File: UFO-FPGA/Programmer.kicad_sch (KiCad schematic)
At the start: 41 parts, among them U2 FT2232HL, U3 ASDMB-12MHz

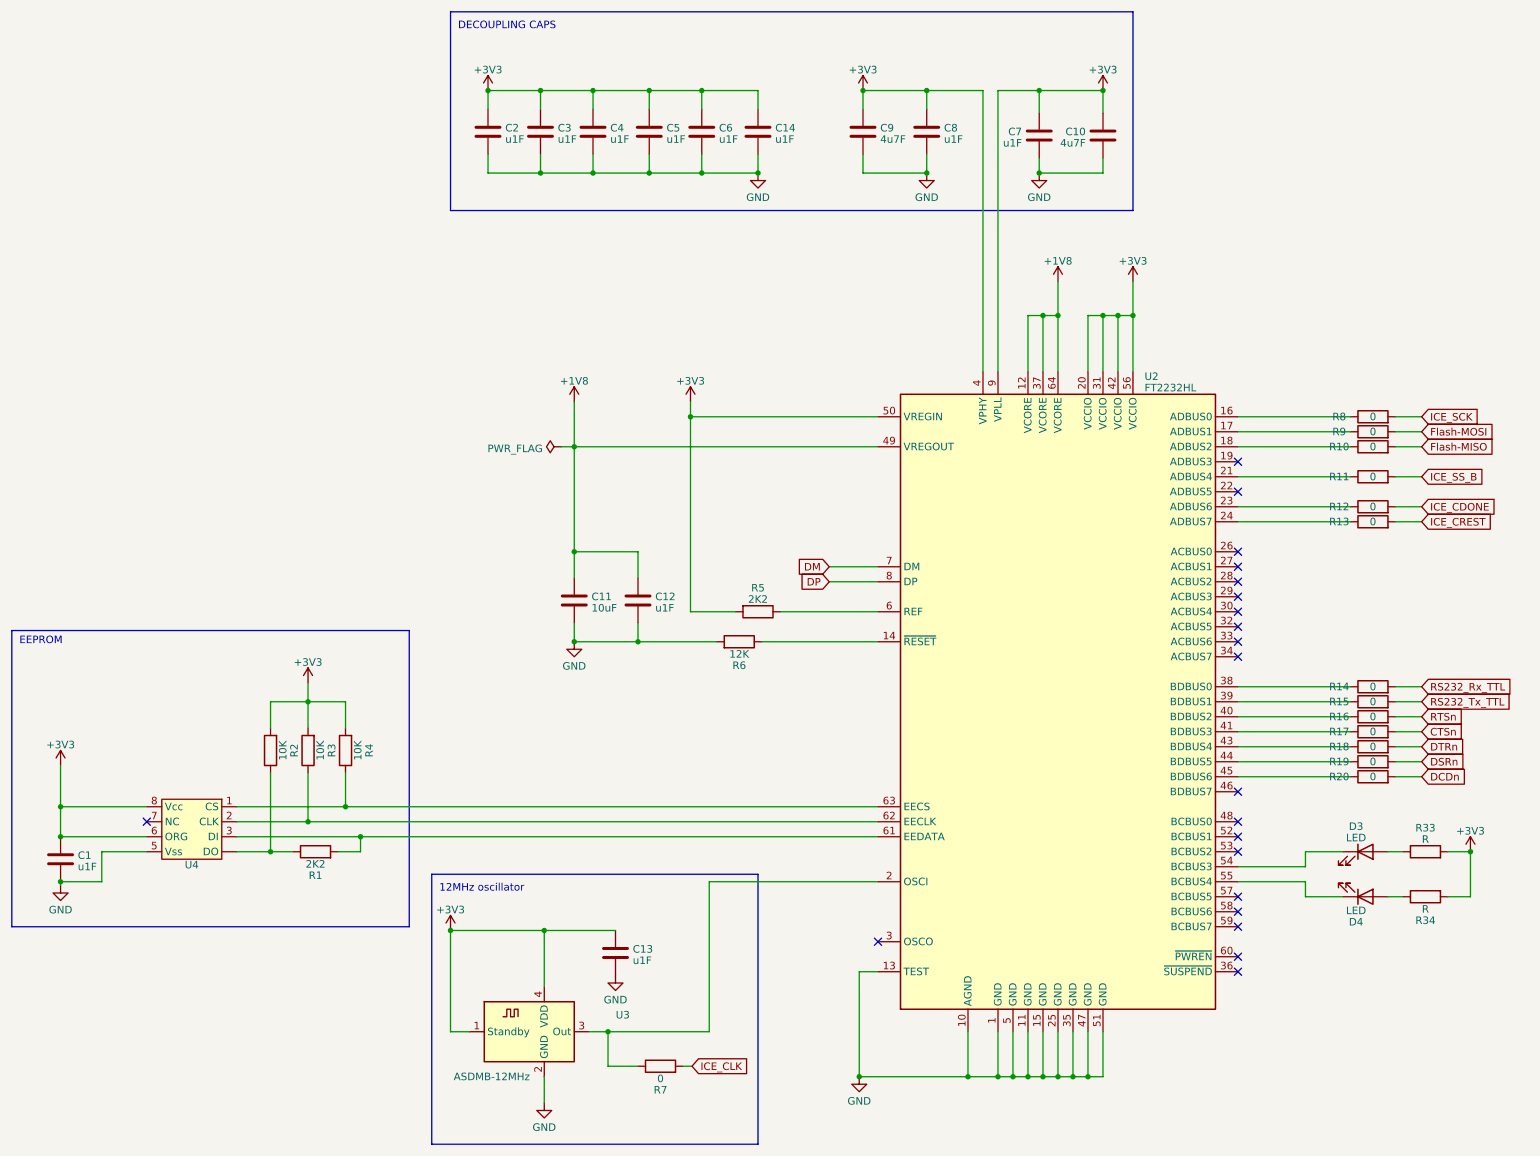
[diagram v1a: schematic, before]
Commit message: Labels and schametic changes
Updated Power schematic
Added labes for the different nets
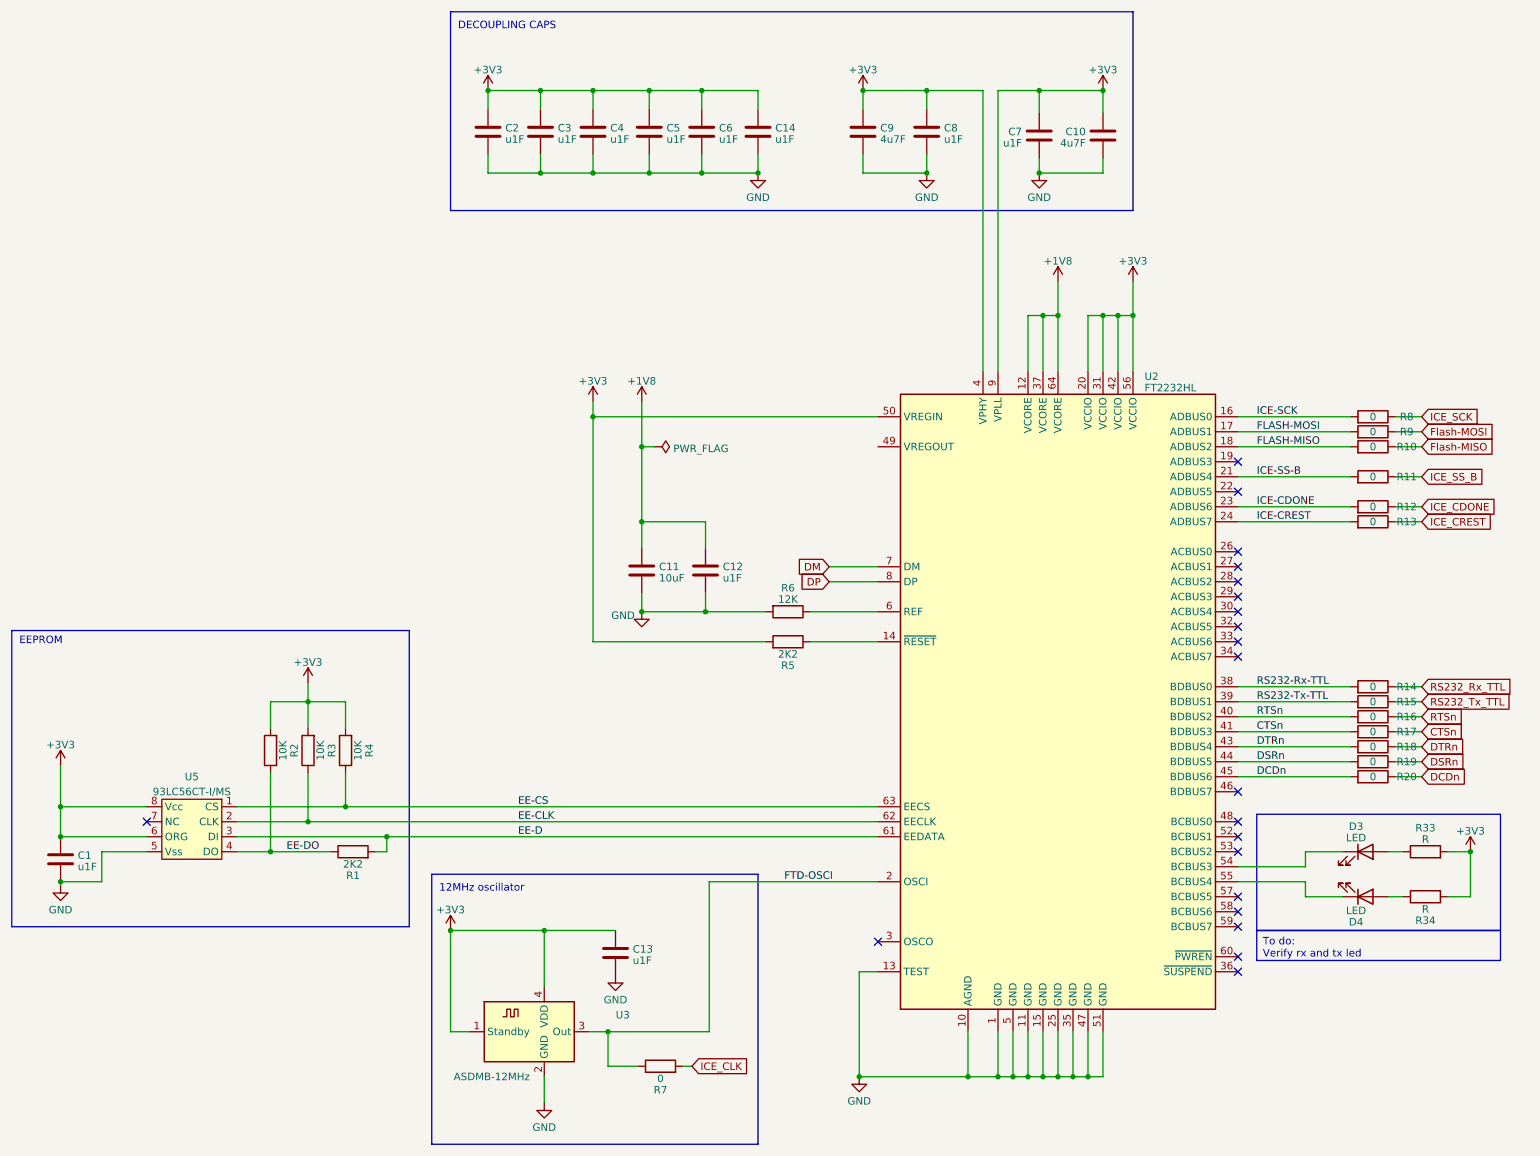
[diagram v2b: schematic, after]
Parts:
- removed U4: ~, Package_SO:MSOP-8-1EP_3x3mm_P0.65mm_EP1.68x1.88mm, symbol EXTRA-PARTS:93LC56CT-I/MS
- added U5: 93LC56CT-I/MS, symbol UFO_PARTS:93LC56CT-I/MS
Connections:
- net +1V8: no longer U2.49 (VREGOUT)
- net +3V3: now also U5.6 (ORG), U5.8 (Vcc)
- net CTSn: now also R17.1, U2.41 (BDBUS3)
- net DCDn: now also R20.1, U2.45 (BDBUS6)
- net DSRn: now also R19.1, U2.44 (BDBUS5)
- net DTRn: now also R18.1, U2.43 (BDBUS4)
- net Flash-MISO: now also R10.1; no longer R10.2
- net Flash-MOSI: now also R9.1; no longer R9.2
- net GND: now also U5.5 (Vss)
- net ICE_CDONE: now also R12.1; no longer R12.2
- net ICE_CREST: now also R13.1; no longer R13.2
- net ICE_SCK: now also R8.1; no longer R8.2
- net ICE_SS_B: now also R11.1; no longer R11.2
- net RS232_Rx_TTL: now also R14.1; no longer R14.2
- net RS232_Tx_TTL: now also R15.1; no longer R15.2
- net RTSn: now also R16.1, U2.40 (BDBUS2)
- net ICE-CREST: now reaches U2.24 (ADBUS7)
- net ICE-CREST: now also R13.2; no longer R13.1
- net RS232-Tx-TTL: now reaches U2.39 (BDBUS1)
- net RS232-Tx-TTL: now also R15.2; no longer R15.1
- net ICE-SS-B: now reaches U2.21 (ADBUS4)
- net ICE-SS-B: now also R11.2; no longer R11.1
- net RS232-Rx-TTL: now reaches U2.38 (BDBUS0)
- net RS232-Rx-TTL: now also R14.2; no longer R14.1
- net EE-DO: now reaches R1.1, R2.1
- net EE-DO: now also U5.4 (DO)
- net EE-D: now reaches R1.2, U2.61 (EEDATA)
- net EE-D: now also U5.3 (DI)
- net FLASH-MOSI: now reaches U2.17 (ADBUS1)
- net FLASH-MOSI: now also R9.2; no longer R9.1
- net FLASH-MISO: now reaches U2.18 (ADBUS2)
- net FLASH-MISO: now also R10.2; no longer R10.1
- net ICE-SCK: now reaches U2.16 (ADBUS0)
- net ICE-SCK: now also R8.2; no longer R8.1
- net at R6.1: now also U2.6 (REF); no longer U2.14 (~{RESET})
- net FTD-OSCI: now reaches R7.1, U2.2 (OSCI), U3.3 (Out)
- net ICE-CDONE: now reaches U2.23 (ADBUS6)
- net ICE-CDONE: now also R12.2; no longer R12.1
- net at R5.1: now also U2.14 (~{RESET}); no longer U2.6 (REF)
- net EE-CS: now reaches R4.1, U2.63 (EECS)
- net EE-CS: now also U5.1 (CS)
- net EE-CLK: now reaches R3.1, U2.62 (EECLK)
- net EE-CLK: now also U5.2 (CLK)
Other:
- moved on the sheet: C11, C12, R1, R10, R11, R12, R13, R14, R15, R16, R17, R18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

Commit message: Revision
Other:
- company: (none) -> Universal-Field-Objects
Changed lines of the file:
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@@
   (paper "A3")
   (title_block
-    (date "2023-04-22")
-    (rev "V0.1")
+    (date "2023-04-25")
+    (rev "V0.5")
+    (company "Universal-Field-Objects")
   )
   (junction (at 264.16 64.135) (diameter 0) (color 0 0 0 0)

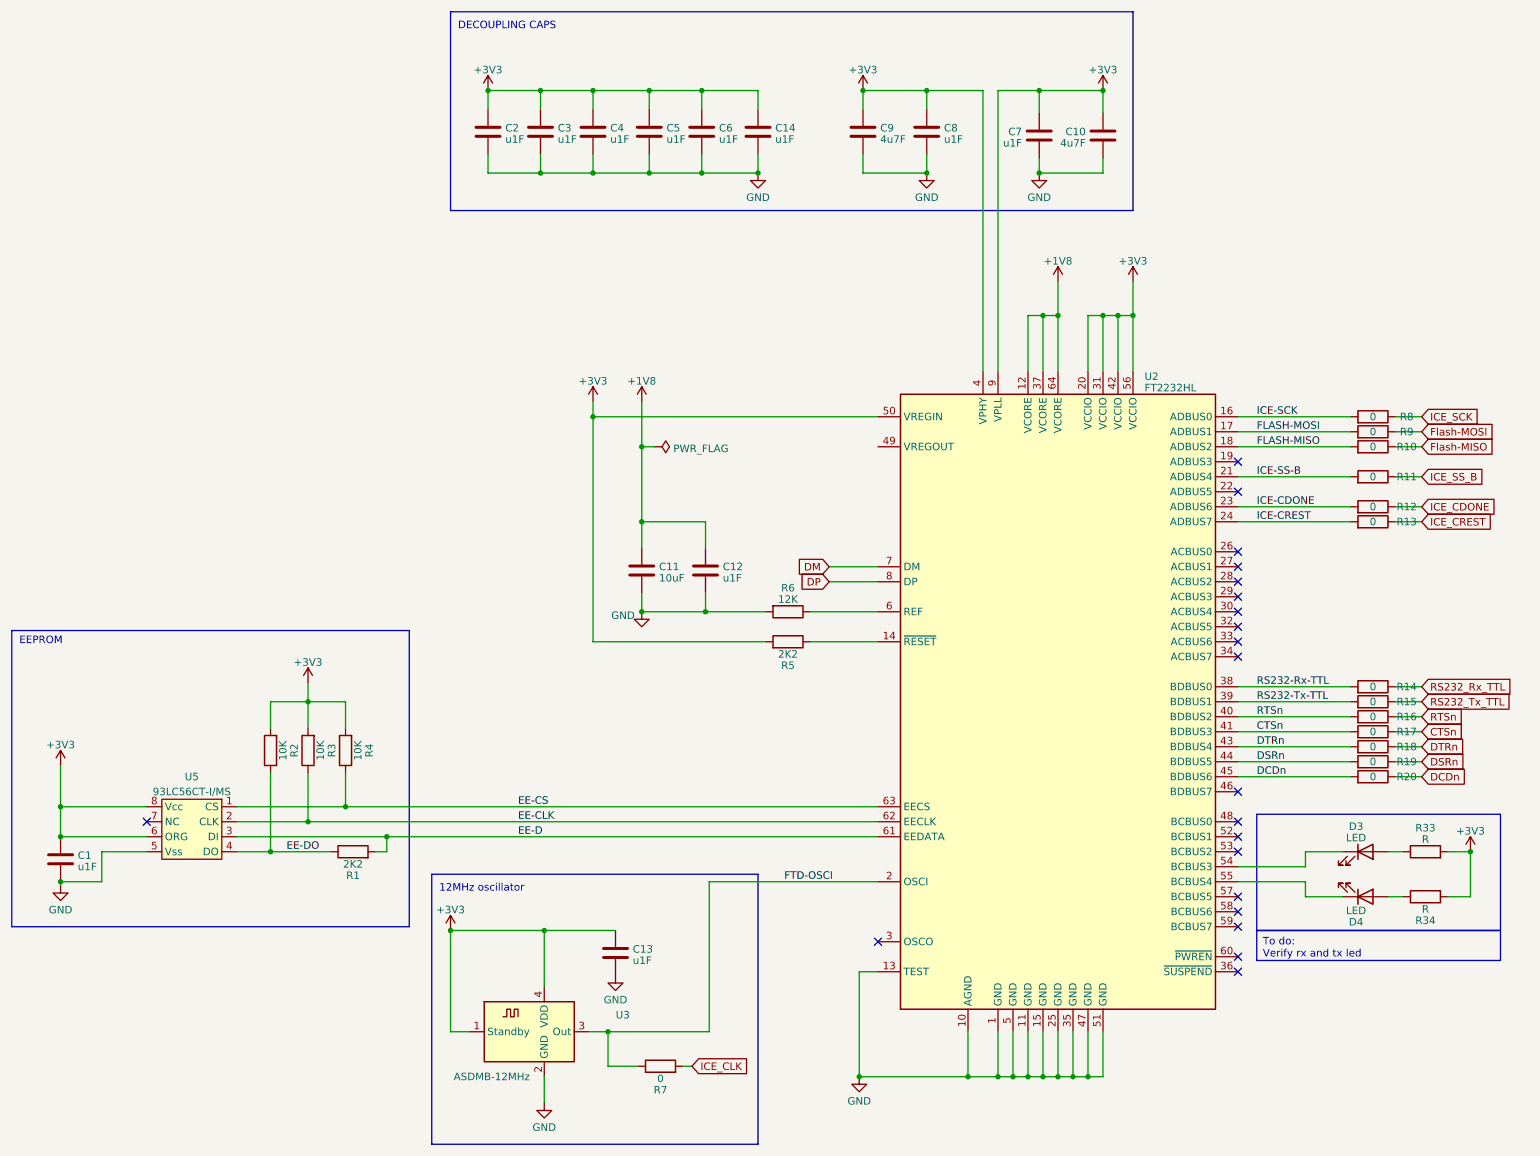
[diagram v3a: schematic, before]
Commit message: PCB and footprint
Added foorprints and moved on pcb layout
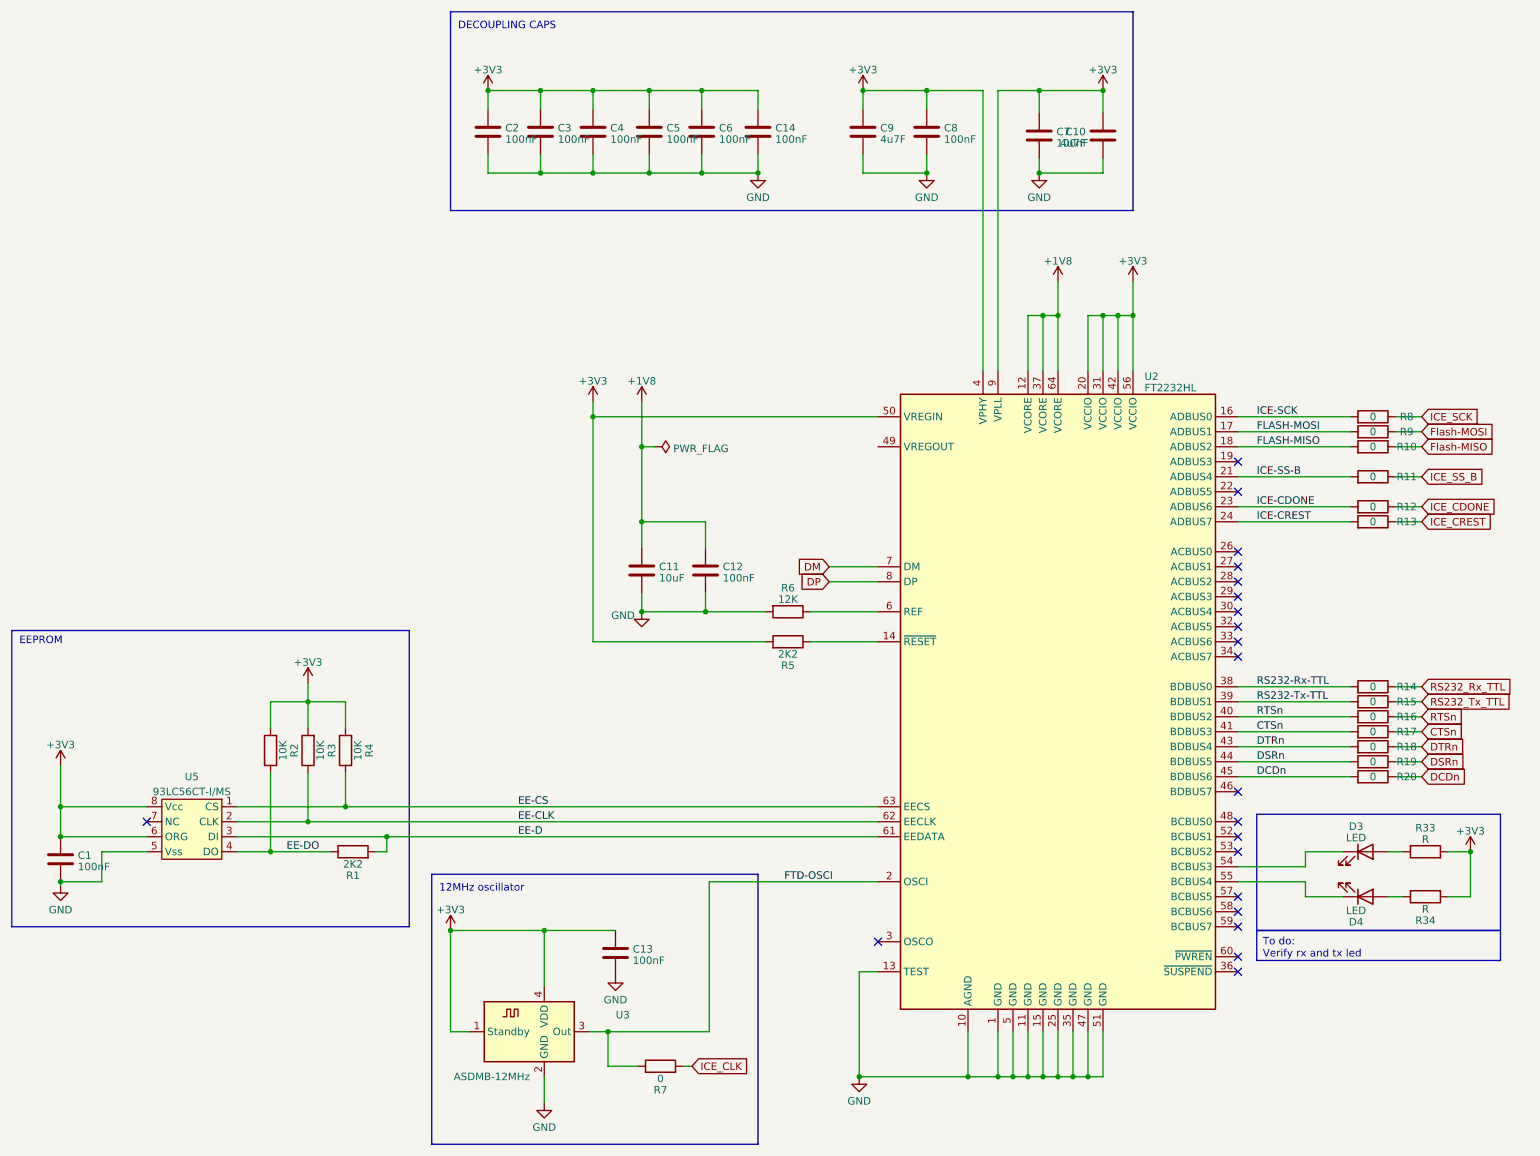
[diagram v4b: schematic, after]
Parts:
- C1, C12, C13, C14, C2, C3, C4, C5, C6, C7, C8: value u1F -> 100nF
- U5: footprint (none) -> Package_SO:MSOP-8_3x3mm_P0.65mm
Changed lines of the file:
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@@
       (effects (font (size 1.27 1.27)) (justify left))
     )
-    (property "Value" "u1F" (at 178.181 34.2973 0)
+    (property "Value" "100nF" (at 178.181 34.2973 0)
       (effects (font (size 1.27 1.27)) (justify left))
     )
@@
   (symbol (lib_id "Device:C") (at 250.825 33.655 0) (mirror y) (unit 1)
     (in_bom yes) (on_board yes) (dnp no) (fields_autoplaced)
-    (property "Reference" "C7" (at 247.904 33.0113 0)
-      (effects (font (size 1.27 1.27)) (justify left))
-    )
-    (property "Value" "u1F" (at 247.904 34.9323 0)
-      (effects (font (size 1.27 1.27)) (justify left))
+    (property "Reference" "C7" (at 253.746 33.0113 0)
+      (effects (font (size 1.27 1.27)) (justify right))
+    )
+    (property "Value" "100nF" (at 253.746 34.9323 0)
+      (effects (font (size 1.27 1.27)) (justify right))
     )
     (property "Footprint" "" (at 249.8598 37.465 0)
@@
       (effects (font (size 1.27 1.27)) (justify left))
     )
-    (property "Value" "u1F" (at 169.291 34.2973 0)
+    (property "Value" "100nF" (at 169.291 34.2973 0)
       (effects (font (size 1.27 1.27)) (justify left))
     )
@@
       (effects (font (size 1.27 1.27)) (justify left))
     )
-    (property "Value" "u1F" (at 196.596 34.2973 0)
+    (property "Value" "100nF" (at 196.596 34.2973 0)
       (effects (font (size 1.27 1.27)) (justify left))
     )
@@
       (effects (font (size 1.27 1.27)) (justify left))
     )
-    (property "Value" "u1F" (at 197.231 108.5923 0)
+    (property "Value" "100nF" (at 197.231 108.5923 0)
       (effects (font (size 1.27 1.27)) (justify left))
     )
@@
       (effects (font (size 1.27 1.27)) (justify left))
     )
-    (property "Value" "u1F" (at 206.121 34.2973 0)
+    (property "Value" "100nF" (at 206.121 34.2973 0)
       (effects (font (size 1.27 1.27)) (justify left))
     )
@@
       (effects (font (size 1.27 1.27)) (justify left))
     )
-    (property "Value" "u1F" (at 88.011 157.4873 0)
+    (property "Value" "100nF" (at 88.011 157.4873 0)
       (effects (font (size 1.27 1.27)) (justify left))
     )
@@
       (effects (font (size 1.27 1.27)) (justify left))
     )
-    (property "Value" "u1F" (at 181.991 173.3623 0)
+    (property "Value" "100nF" (at 181.991 173.3623 0)
       (effects (font (size 1.27 1.27)) (justify left))
     )
@@
       (effects (font (size 1.27 1.27)))
     )
-    (property "Footprint" "" (at 107.315 144.78 0)
+    (property "Footprint" "Package_SO:MSOP-8_3x3mm_P0.65mm" (at 107.315 144.78 0)
       (effects (font (size 1.27 1.27)) hide)
     )
@@
       (effects (font (size 1.27 1.27)) (justify left))
     )
-    (property "Value" "u1F" (at 160.401 34.2973 0)
+    (property "Value" "100nF" (at 160.401 34.2973 0)
       (effects (font (size 1.27 1.27)) (justify left))
     )
@@
       (effects (font (size 1.27 1.27)) (justify left))
     )
-    (property "Value" "u1F" (at 234.696 34.2973 0)
+    (property "Value" "100nF" (at 234.696 34.2973 0)
       (effects (font (size 1.27 1.27)) (justify left))
     )
@@
       (effects (font (size 1.27 1.27)) (justify left))
     )
-    (property "Value" "u1F" (at 187.706 34.2973 0)
-      (effects (font (size 1.27 1.27)) (justify left))
-    )
+    (property "Value" "100nF" (at 187.706 34.2973 0)
+      (effects (font (size 1.27 1.27)) (justify left))
+    )

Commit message: edge cuts
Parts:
- D3: value LED -> RXLED
- D4: value LED -> TXLED
- R33, R34: value R -> 220R
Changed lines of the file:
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@@
     (fill (type none))
-  )
-  (text_box "To do:\nVerify rx and tx led"
-    (at 287.655 168.275 0) (size 41.275 5.08)
-    (stroke (width 0) (type default))
-    (fill (type none))
-    (effects (font (size 1.27 1.27)) (justify left top))
   )
   (text "12MHz oscillator" (at 149.225 161.925 0)
@@
       (effects (font (size 1.27 1.27)))
     )
-    (property "Value" "R" (at 316.23 152.8351 90)
+    (property "Value" "220R" (at 316.23 152.8351 90)
       (effects (font (size 1.27 1.27)))
     )
@@
       (effects (font (size 1.27 1.27)))
     )
-    (property "Value" "LED" (at 304.4825 164.9189 0)
+    (property "Value" "TXLED" (at 304.4825 164.9189 0)
       (effects (font (size 1.27 1.27)))
     )
@@
       (effects (font (size 1.27 1.27)))
     )
-    (property "Value" "R" (at 316.23 164.6649 90)
+    (property "Value" "220R" (at 316.23 164.6649 90)
       (effects (font (size 1.27 1.27)))
     )
@@
       (effects (font (size 1.27 1.27)))
     )
-    (property "Value" "LED" (at 304.4825 152.5811 0)
-      (effects (font (size 1.27 1.27)))
-    )
+    (property "Value" "RXLED" (at 304.4825 152.5811 0)
+      (effects (font (size 1.27 1.27)))
+    )
